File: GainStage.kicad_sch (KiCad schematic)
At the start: 32 parts, among them SW1 SW_DPDT_x2, U1 TL072

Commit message: using smt caps and resistors
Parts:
- C10, C12, C13, C3, C4, C5, C6, C7, C8, C9: footprint ECE319K:C_Axial_200mil -> Capacitor_SMD:C_0805_2012Metric_Pad1.18x1.45mm_HandSolder
- C11: footprint ECE319K:CP_Radial_Tantal200mil -> Capacitor_SMD:C_0805_2012Metric_Pad1.18x1.45mm_HandSolder
- R10, R11, R12, R13, R14, R15, R16, R17, R18, R30, R5, R6, R7, R8, R9: footprint Resistor_THT:R_Axial_DIN0207_L6.3mm_D2.5mm_P10.16mm_Horizontal -> Resistor_SMD:R_0805_2012Metric_Pad1.20x1.40mm_HandSolder
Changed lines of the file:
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@@
 			)
 		)
-		(property "Footprint" "ECE319K:C_Axial_200mil"
+		(property "Footprint" "Capacitor_SMD:C_0805_2012Metric_Pad1.18x1.45mm_HandSolder"
 			(at 165.735 75.8952 0)
 			(effects
@@
 			)
 		)
-		(property "Footprint" "Resistor_THT:R_Axial_DIN0207_L6.3mm_D2.5mm_P10.16mm_Horizontal"
+		(property "Footprint" "Resistor_SMD:R_0805_2012Metric_Pad1.20x1.40mm_HandSolder"
 			(at 43.942 97.79 90)
 			(effects
@@
 			)
 		)
-		(property "Footprint" "Resistor_THT:R_Axial_DIN0207_L6.3mm_D2.5mm_P10.16mm_Horizontal"
+		(property "Footprint" "Resistor_SMD:R_0805_2012Metric_Pad1.20x1.40mm_HandSolder"
 			(at 116.84 22.987 90)
 			(effects
@@
 			)
 		)
-		(property "Footprint" "ECE319K:C_Axial_200mil"
+		(property "Footprint" "Capacitor_SMD:C_0805_2012Metric_Pad1.18x1.45mm_HandSolder"
 			(at 76.2 71.4248 0)
 			(effects
@@
 			)
 		)
-		(property "Footprint" "ECE319K:C_Axial_200mil"
+		(property "Footprint" "Capacitor_SMD:C_0805_2012Metric_Pad1.18x1.45mm_HandSolder"
 			(at 55.5498 93.98 0)
 			(effects
@@
 			)
 		)
-		(property "Footprint" "Resistor_THT:R_Axial_DIN0207_L6.3mm_D2.5mm_P10.16mm_Horizontal"
+		(property "Footprint" "Resistor_SMD:R_0805_2012Metric_Pad1.20x1.40mm_HandSolder"
 			(at 196.342 105.41 90)
 			(effects
@@
 			)
 		)
-		(property "Footprint" "ECE319K:C_Axial_200mil"
+		(property "Footprint" "Capacitor_SMD:C_0805_2012Metric_Pad1.18x1.45mm_HandSolder"
 			(at 125.73 75.8952 0)
 			(effects
@@
 			)
 		)
-		(property "Footprint" "Resistor_THT:R_Axial_DIN0207_L6.3mm_D2.5mm_P10.16mm_Horizontal"
+		(property "Footprint" "Resistor_SMD:R_0805_2012Metric_Pad1.20x1.40mm_HandSolder"
 			(at 95.25 104.267 90)
 			(effects
@@
 			)
 		)
-		(property "Footprint" "Resistor_THT:R_Axial_DIN0207_L6.3mm_D2.5mm_P10.16mm_Horizontal"
+		(property "Footprint" "Resistor_SMD:R_0805_2012Metric_Pad1.20x1.40mm_HandSolder"
 			(at 72.39 83.693 90)
 			(effects
@@
 			)
 		)
-		(property "Footprint" "ECE319K:C_Axial_200mil"
+		(property "Footprint" "Capacitor_SMD:C_0805_2012Metric_Pad1.18x1.45mm_HandSolder"
 			(at 176.8602 93.345 0)
 			(effects
@@
 			)
 		)
-		(property "Footprint" "ECE319K:C_Axial_200mil"
+		(property "Footprint" "Capacitor_SMD:C_0805_2012Metric_Pad1.18x1.45mm_HandSolder"
 			(at 62.865 80.9498 0)
 			(effects
@@
 			)
 		)
-		(property "Footprint" "ECE319K:CP_Radial_Tantal200mil"
+		(property "Footprint" "Capacitor_SMD:C_0805_2012Metric_Pad1.18x1.45mm_HandSolder"
 			(at 126.6952 35.56 0)
 			(effects
@@
 			)
 		)
-		(property "Footprint" "Resistor_THT:R_Axial_DIN0207_L6.3mm_D2.5mm_P10.16mm_Horizontal"
+		(property "Footprint" "Resistor_SMD:R_0805_2012Metric_Pad1.20x1.40mm_HandSolder"
 			(at 85.852 94.615 90)
 			(effects
@@
 			)
 		)
-		(property "Footprint" "Resistor_THT:R_Axial_DIN0207_L6.3mm_D2.5mm_P10.16mm_Horizontal"
+		(property "Footprint" "Resistor_SMD:R_0805_2012Metric_Pad1.20x1.40mm_HandSolder"
 			(at 181.61 73.152 90)
 			(effects
@@
 			)
 		)
-		(property "Footprint" "Resistor_THT:R_Axial_DIN0207_L6.3mm_D2.5mm_P10.16mm_Horizontal"
+		(property "Footprint" "Resistor_SMD:R_0805_2012Metric_Pad1.20x1.40mm_HandSolder"
 			(at 140.97 73.152 90)
 			(effects
@@
 			)
 		)
-		(property "Footprint" "Resistor_THT:R_Axial_DIN0207_L6.3mm_D2.5mm_P10.16mm_Horizontal"
+		(property "Footprint" "Resistor_SMD:R_0805_2012Metric_Pad1.20x1.40mm_HandSolder"
 			(at 127 54.102 90)
 			(effects
@@
 			)
 		)
-		(property "Footprint" "Resistor_THT:R_Axial_DIN0207_L6.3mm_D2.5mm_P10.16mm_Horizontal"
+		(property "Footprint" "Resistor_SMD:R_0805_2012Metric_Pad1.20x1.40mm_HandSolder"
 			(at 49.022 121.92 90)
 			(effects
@@
 			)
 		)
-		(property "Footprint" "ECE319K:C_Axial_200mil"
+		(property "Footprint" "Capacitor_SMD:C_0805_2012Metric_Pad1.18x1.45mm_HandSolder"
 			(at 105.41 117.8052 0)
 			(effects
@@
 			)
 		)
-		(property "Footprint" "Resistor_THT:R_Axial_DIN0207_L6.3mm_D2.5mm_P10.16mm_Horizontal"
+		(property "Footprint" "Resistor_SMD:R_0805_2012Metric_Pad1.20x1.40mm_HandSolder"
 			(at 186.817 97.155 90)
 			(effects
@@
 			)
 		)
-		(property "Footprint" "Resistor_THT:R_Axial_DIN0207_L6.3mm_D2.5mm_P10.16mm_Horizontal"
+		(property "Footprint" "Resistor_SMD:R_0805_2012Metric_Pad1.20x1.40mm_HandSolder"
 			(at 133.985 22.987 90)
 			(effects
@@
 			)
 		)
-		(property "Footprint" "ECE319K:C_Axial_200mil"
+		(property "Footprint" "Capacitor_SMD:C_0805_2012Metric_Pad1.18x1.45mm_HandSolder"
 			(at 91.44 117.8052 0)
 			(effects
@@
 			)
 		)
-		(property "Footprint" "ECE319K:C_Axial_200mil"
+		(property "Footprint" "Capacitor_SMD:C_0805_2012Metric_Pad1.18x1.45mm_HandSolder"
 			(at 59.3598 109.855 0)
 			(effects
@@
 			)
 		)
-		(property "Footprint" "Resistor_THT:R_Axial_DIN0207_L6.3mm_D2.5mm_P10.16mm_Horizontal"
+		(property "Footprint" "Resistor_SMD:R_0805_2012Metric_Pad1.20x1.40mm_HandSolder"
 			(at 58.547 130.175 90)
 			(effects
@@
 			)
 		)
-		(property "Footprint" "Resistor_THT:R_Axial_DIN0207_L6.3mm_D2.5mm_P10.16mm_Horizontal"
+		(property "Footprint" "Resistor_SMD:R_0805_2012Metric_Pad1.20x1.40mm_HandSolder"
 			(at 174.117 102.87 90)
 			(effects
@@
 			)
 		)
-		(property "Footprint" "Resistor_THT:R_Axial_DIN0207_L6.3mm_D2.5mm_P10.16mm_Horizontal"
+		(property "Footprint" "Resistor_SMD:R_0805_2012Metric_Pad1.20x1.40mm_HandSolder"
 			(at 109.22 104.267 90)
 			(effects
@@
 			)
 		)
-		(property "Footprint" "ECE319K:C_Axial_200mil"
+		(property "Footprint" "Capacitor_SMD:C_0805_2012Metric_Pad1.18x1.45mm_HandSolder"
 			(at 197.1548 85.09 0)
 			(effects

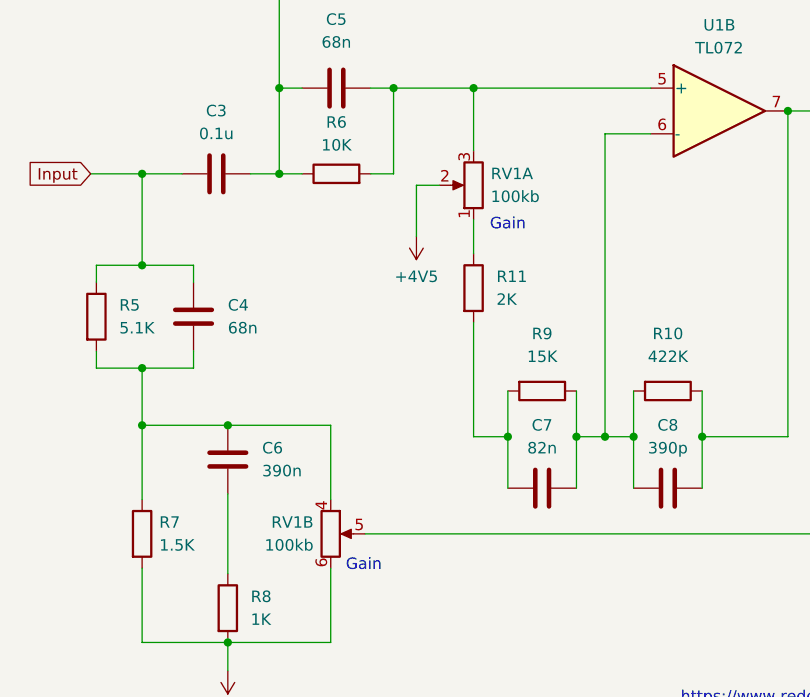
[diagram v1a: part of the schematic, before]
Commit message: change metal film resistor footprint
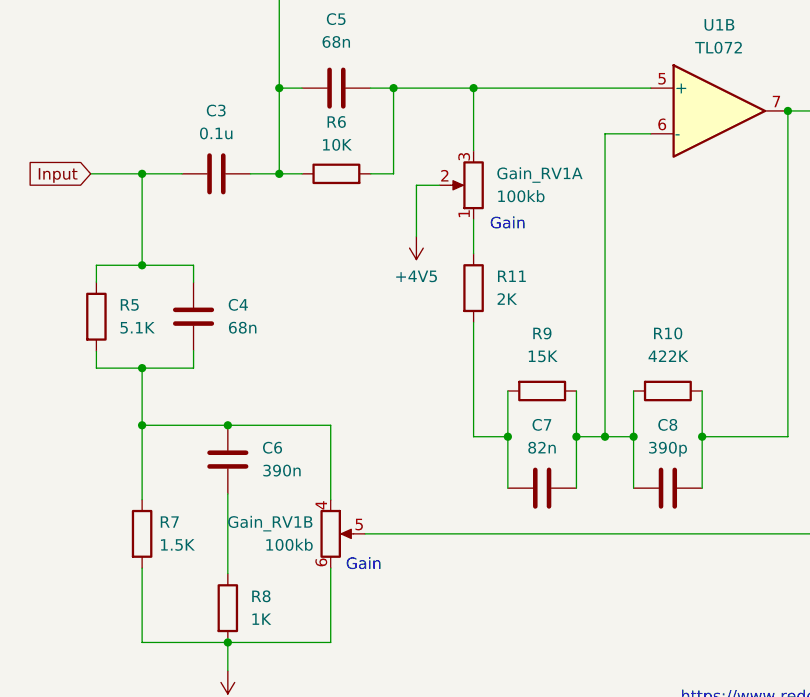
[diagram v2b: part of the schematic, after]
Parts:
- R10, R11, R18, R5, R6, R7: footprint Resistor_SMD:R_0805_2012Metric_Pad1.20x1.40mm_HandSolder -> Resistor_THT:R_Axial_DIN0207_L6.3mm_D2.5mm_P10.16mm_Horizontal
- U1: footprint ECE319K:DIP-8_W7.62mm_LongPads -> Package_SO:SO-8_3.9x4.9mm_P1.27mm
- renumbered RV1 to Gain_RV1
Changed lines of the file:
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@@
 			)
 		)
-		(property "Footprint" "Resistor_SMD:R_0805_2012Metric_Pad1.20x1.40mm_HandSolder"
+		(property "Footprint" "Resistor_THT:R_Axial_DIN0207_L6.3mm_D2.5mm_P10.16mm_Horizontal"
 			(at 43.942 97.79 90)
 			(effects
@@
 			)
 		)
-		(property "Footprint" "ECE319K:DIP-8_W7.62mm_LongPads"
+		(property "Footprint" "Package_SO:SO-8_3.9x4.9mm_P1.27mm"
 			(at 114.935 74.93 0)
 			(effects
@@
 			)
 		)
-		(property "Footprint" "Resistor_SMD:R_0805_2012Metric_Pad1.20x1.40mm_HandSolder"
+		(property "Footprint" "Resistor_THT:R_Axial_DIN0207_L6.3mm_D2.5mm_P10.16mm_Horizontal"
 			(at 196.342 105.41 90)
 			(effects
@@
 			)
 		)
-		(property "Footprint" "Resistor_SMD:R_0805_2012Metric_Pad1.20x1.40mm_HandSolder"
+		(property "Footprint" "Resistor_THT:R_Axial_DIN0207_L6.3mm_D2.5mm_P10.16mm_Horizontal"
 			(at 72.39 83.693 90)
 			(effects
@@
 			)
 		)
-		(property "Footprint" "Resistor_SMD:R_0805_2012Metric_Pad1.20x1.40mm_HandSolder"
+		(property "Footprint" "Resistor_THT:R_Axial_DIN0207_L6.3mm_D2.5mm_P10.16mm_Horizontal"
 			(at 85.852 94.615 90)
 			(effects
@@
 		(dnp no)
 		(fields_autoplaced yes)
-		(property "Reference" "RV1"
-			(at 89.535 81.9149 0)
+		(property "Reference" "Gain_RV1"
+			(at 90.17 81.9149 0)
 			(effects
 				(font
@@
 		)
 		(property "Value" "100kb"
-			(at 89.535 84.4549 0)
+			(at 90.17 84.4549 0)
 			(effects
 				(font
@@
 			(project "KlonePedal"
 				(path "/9e3f79d9-06b6-4799-a8c0-00f1612ca30b/0a08b33d-ca03-4908-ad3a-32123bc769f4"
-					(reference "RV1")
+					(reference "Gain_RV1")
 					(unit 1)
 				)
@@
 			)
 		)
-		(property "Footprint" "Resistor_SMD:R_0805_2012Metric_Pad1.20x1.40mm_HandSolder"
+		(property "Footprint" "Resistor_THT:R_Axial_DIN0207_L6.3mm_D2.5mm_P10.16mm_Horizontal"
 			(at 49.022 121.92 90)
 			(effects
@@
 		(dnp no)
 		(fields_autoplaced yes)
-		(property "Reference" "RV1"
+		(property "Reference" "Gain_RV1"
 			(at 69.85 120.6499 0)
 			(effects
@@
 			(project "KlonePedal"
 				(path "/9e3f79d9-06b6-4799-a8c0-00f1612ca30b/0a08b33d-ca03-4908-ad3a-32123bc769f4"
-					(reference "RV1")
+					(reference "Gain_RV1")
 					(unit 2)
 				)
@@
 			)
 		)
-		(property "Footprint" "Resistor_SMD:R_0805_2012Metric_Pad1.20x1.40mm_HandSolder"
+		(property "Footprint" "Resistor_THT:R_Axial_DIN0207_L6.3mm_D2.5mm_P10.16mm_Horizontal"
 			(at 109.22 104.267 90)
 			(effects

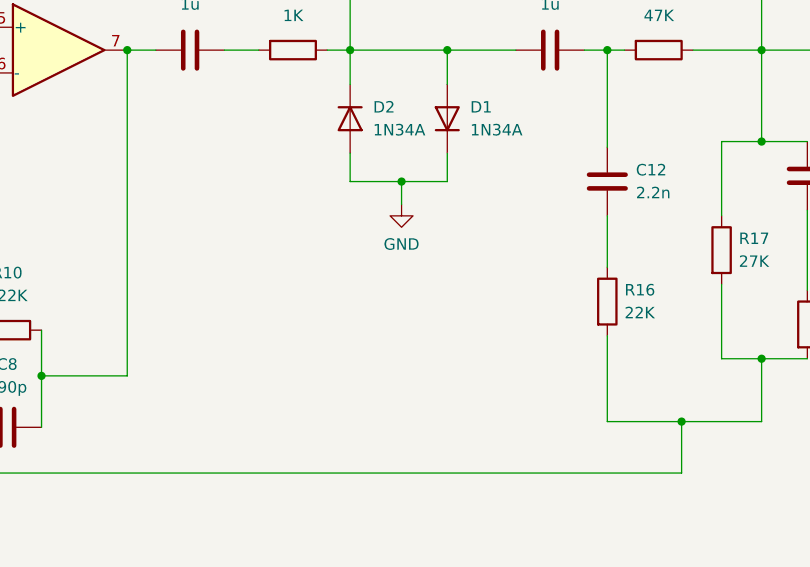
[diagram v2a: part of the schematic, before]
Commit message: add all smd components
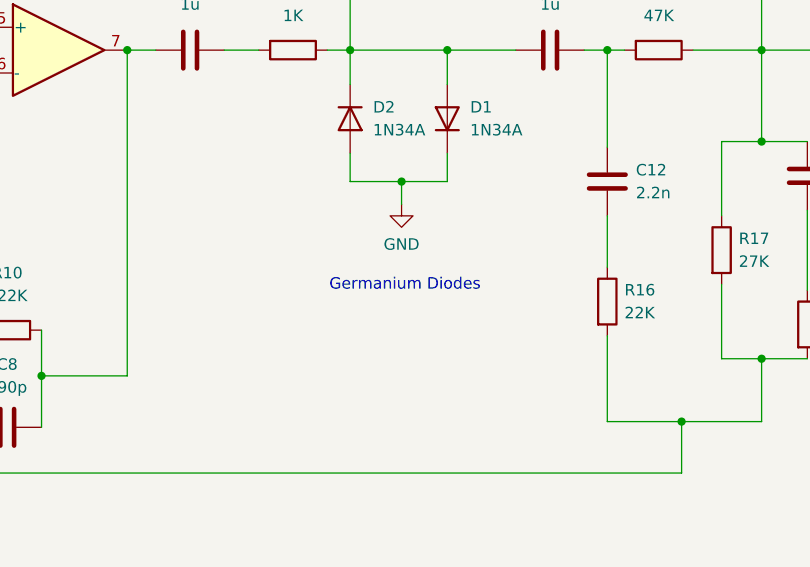
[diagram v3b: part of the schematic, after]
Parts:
- R10, R11, R18, R5, R6, R7: footprint Resistor_THT:R_Axial_DIN0207_L6.3mm_D2.5mm_P10.16mm_Horizontal -> Resistor_SMD:R_0805_2012Metric_Pad1.20x1.40mm_HandSolder
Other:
- note added: "Germanium Diodes"
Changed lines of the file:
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@@
 	(generator_version "9.0")
 	(paper "A4")
+	(text "Germanium Diodes"
+		(exclude_from_sim no)
+		(at 153.416 101.092 0)
+		(effects
+			(font
+				(size 1.27 1.27)
+			)
+		)
+	)
 	(text "Gain\n"
 		(exclude_from_sim no)
@@
 			)
 		)
-		(property "Footprint" "Resistor_THT:R_Axial_DIN0207_L6.3mm_D2.5mm_P10.16mm_Horizontal"
+		(property "Footprint" "Resistor_SMD:R_0805_2012Metric_Pad1.20x1.40mm_HandSolder"
 			(at 43.942 97.79 90)
 			(effects
@@
 			)
 		)
-		(property "Footprint" "Resistor_THT:R_Axial_DIN0207_L6.3mm_D2.5mm_P10.16mm_Horizontal"
+		(property "Footprint" "Resistor_SMD:R_0805_2012Metric_Pad1.20x1.40mm_HandSolder"
 			(at 196.342 105.41 90)
 			(effects
@@
 			)
 		)
-		(property "Footprint" "Resistor_THT:R_Axial_DIN0207_L6.3mm_D2.5mm_P10.16mm_Horizontal"
+		(property "Footprint" "Resistor_SMD:R_0805_2012Metric_Pad1.20x1.40mm_HandSolder"
 			(at 72.39 83.693 90)
 			(effects
@@
 			)
 		)
-		(property "Footprint" "Resistor_THT:R_Axial_DIN0207_L6.3mm_D2.5mm_P10.16mm_Horizontal"
+		(property "Footprint" "Resistor_SMD:R_0805_2012Metric_Pad1.20x1.40mm_HandSolder"
 			(at 85.852 94.615 90)
 			(effects
@@
 			)
 		)
-		(property "Footprint" "Resistor_THT:R_Axial_DIN0207_L6.3mm_D2.5mm_P10.16mm_Horizontal"
+		(property "Footprint" "Resistor_SMD:R_0805_2012Metric_Pad1.20x1.40mm_HandSolder"
 			(at 49.022 121.92 90)
 			(effects
@@
 			)
 		)
-		(property "Footprint" "Resistor_THT:R_Axial_DIN0207_L6.3mm_D2.5mm_P10.16mm_Horizontal"
+		(property "Footprint" "Resistor_SMD:R_0805_2012Metric_Pad1.20x1.40mm_HandSolder"
 			(at 109.22 104.267 90)
 			(effects

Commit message: initial layout
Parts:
- removed SW1: SW_DPDT_x2, Connector_Wire:SolderWire-0.1sqmm_1x03_P3.6mm_D0.4mm_OD1mm, symbol Switch:SW_DPDT_x2
- added J3: SW1B_DPDT_x2, Connector_JST:JST_XH_S3B-XH-A_1x03_P2.50mm_Horizontal, symbol Connector_Generic:Conn_01x03
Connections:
- net GND: now also J3.2 (Pin_2)
- net at C10.2, D1.2 (A), D2.1 (K)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: now also J3.3 (Pin_3)
- net at D6.1 (K): now also J3.1 (Pin_1)
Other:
- note added: "1/4"
- note added: "2/5"
- note added: "3/6"
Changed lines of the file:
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@@
 		)
 	)
+	(text "3/6"
+		(exclude_from_sim no)
+		(at 150.114 49.784 0)
+		(effects
+			(font
+				(size 1.27 1.27)
+			)
+		)
+	)
+	(text "1/4"
+		(exclude_from_sim no)
+		(at 150.114 55.118 0)
+		(effects
+			(font
+				(size 1.27 1.27)
+			)
+		)
+	)
 	(text "Gain"
 		(exclude_from_sim no)
@@
 		)
 	)
+	(text "2/5"
+		(exclude_from_sim no)
+		(at 163.322 52.578 0)
+		(effects
+			(font
+				(size 1.27 1.27)
+			)
+		)
+	)
 	(text "tantalum"
 		(exclude_from_sim no)
@@
 	(wire
 		(pts
-			(xy 161.925 53.34) (xy 170.18 53.34)
+			(xy 50.8 109.855) (xy 60.325 109.855)
 		)
 		(stroke
@@
 	(wire
 		(pts
-			(xy 50.8 109.855) (xy 60.325 109.855)
+			(xy 71.755 109.855) (xy 60.325 109.855)
 		)
 		(stroke
@@
 	(wire
 		(pts
-			(xy 71.755 109.855) (xy 60.325 109.855)
+			(xy 113.03 111.125) (xy 113.03 116.84)
 		)
 		(stroke
@@
 	(wire
 		(pts
-			(xy 113.03 111.125) (xy 113.03 116.84)
+			(xy 151.765 58.42) (xy 160.02 58.42)
 		)
 		(stroke
@@
 	(wire
 		(pts
+			(xy 151.765 50.8) (xy 151.765 48.26)
+		)
+		(stroke
+			(width 0)
+			(type default)
+		)
+	)
+	(wire
+		(pts
 			(xy 87.63 72.39) (xy 87.63 79.375)
 		)
@@
 	(wire
 		(pts
+			(xy 151.765 55.88) (xy 151.765 58.42)
+		)
+		(stroke
+			(width 0)
+			(type default)
+		)
+	)
+	(wire
+		(pts
 			(xy 45.72 92.075) (xy 50.8 92.075)
 		)
@@
 	(wire
 		(pts
+			(xy 160.02 53.34) (xy 170.18 53.34)
+		)
+		(stroke
+			(width 0)
+			(type default)
+		)
+	)
+	(wire
+		(pts
 			(xy 87.63 86.995) (xy 87.63 90.805)
 		)
@@
 	(wire
 		(pts
+			(xy 151.765 48.26) (xy 160.02 48.26)
+		)
+		(stroke
+			(width 0)
+			(type default)
+		)
+	)
+	(wire
+		(pts
 			(xy 175.895 116.205) (xy 184.15 116.205)
 		)
@@
 	(wire
 		(pts
+			(xy 160.02 58.42) (xy 160.02 55.88)
+		)
+		(stroke
+			(width 0)
+			(type default)
+		)
+	)
+	(wire
+		(pts
 			(xy 120.65 24.765) (xy 125.73 24.765)
 		)
@@
 	(wire
 		(pts
+			(xy 160.02 48.26) (xy 160.02 50.8)
+		)
+		(stroke
+			(width 0)
+			(type default)
+		)
+	)
+	(wire
+		(pts
 			(xy 147.32 50.8) (xy 147.32 74.93)
 		)
@@
 	)
 	(symbol
-		(lib_id "Switch:SW_DPDT_x2")
-		(at 156.845 53.34 180)
-		(unit 2)
-		(exclude_from_sim no)
-		(in_bom yes)
-		(on_board yes)
-		(dnp no)
-		(fields_autoplaced yes)
-		(property "Reference" "SW1"
-			(at 156.845 44.45 0)
-			(effects
-				(font
-					(size 1.27 1.27)
-				)
-			)
-		)
-		(property "Value" "SW_DPDT_x2"
-			(at 156.845 46.99 0)
-			(effects
-				(font
-					(size 1.27 1.27)
-				)
-			)
-		)
-		(property "Footprint" "Connector_Wire:SolderWire-0.1sqmm_1x03_P3.6mm_D0.4mm_OD1mm"
-			(at 156.845 53.34 0)
-			(effects
-				(font
-					(size 1.27 1.27)
-				)
-				(hide yes)
-			)
-		)
-		(property "Datasheet" "~"
-			(at 156.845 53.34 0)
-			(effects
-				(font
-					(size 1.27 1.27)
-				)
-				(hide yes)
-			)
-		)
-		(property "Description" "Switch, dual pole double throw, separate symbols"
-			(at 156.845 53.34 0)
-			(effects
-				(font
-					(size 1.27 1.27)
-				)
-				(hide yes)
-			)
-		)
-		(pin "2"
-		)
-		(pin "1"
-		)
-		(pin "3"
-		)
-		(pin "5"
-		)
-		(pin "4"
-		)
-		(pin "6"
-		)
-		(instances
-			(project "KlonePedal"
-				(path "/9e3f79d9-06b6-4799-a8c0-00f1612ca30b/0a08b33d-ca03-4908-ad3a-32123bc769f4"
-					(reference "SW1")
-					(unit 2)
-				)
-			)
-		)
-	)
-	(symbol
 		(lib_id "Device:R")
 		(at 140.97 74.93 270)
@@
 					(unit 1)
 				)
+			)
+		)
+	)
+	(symbol
+		(lib_id "Connector_Generic:Conn_01x03")
+		(at 154.94 53.34 180)
+		(unit 1)
+		(exclude_from_sim no)
+		(in_bom yes)
+		(on_board yes)
+		(dnp no)
+		(fields_autoplaced yes)
+		(property "Reference" "J3"
+			(at 154.94 44.45 0)
+			(effects
+				(font
+					(size 1.27 1.27)
+				)
+			)
+		)
+		(property "Value" "SW1B_DPDT_x2"
+			(at 154.94 46.99 0)
+			(effects
+				(font
+					(size 1.27 1.27)
+				)
+			)
+		)
+		(property "Footprint" "Connector_JST:JST_XH_S3B-XH-A_1x03_P2.50mm_Horizontal"
+			(at 154.94 53.34 0)
+			(effects
+				(font
+					(size 1.27 1.27)
+				)
+				(hide yes)
+			)
+		)
+		(property "Datasheet" "~"
+			(at 154.94 53.34 0)
+			(effects
+				(font
+					(size 1.27 1.27)
+				)
+				(hide yes)
+			)
+		)
+		(property "Description" "Generic connector, single row, 01x03, script generated (kicad-library-utils/schlib/autogen/connector/)"
+			(at 154.94 53.34 0)
+			(effects
+				(font
+					(size 1.27 1.27)
+				)
+				(hide yes)
+			)
+		)
+		(pin "1"
+		)
+		(pin "2"
+		)
+		(pin "3"
+		)
+		(instances
+			(project ""
+				(path "/9e3f79d9-06b6-4799-a8c0-00f1612ca30b/0a08b33d-ca03-4908-ad3a-32123bc769f4"
+					(reference "J3")
+					(unit 1)
+				)
